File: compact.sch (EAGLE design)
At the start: 39 parts, among them J3 AVX_6-PIN_009159006061916, J4 CORTEX_DEBUG_PTH, J5 2172034-1, U1 STM32F103C8T6, U2 CJT1117-3.3-SOT223

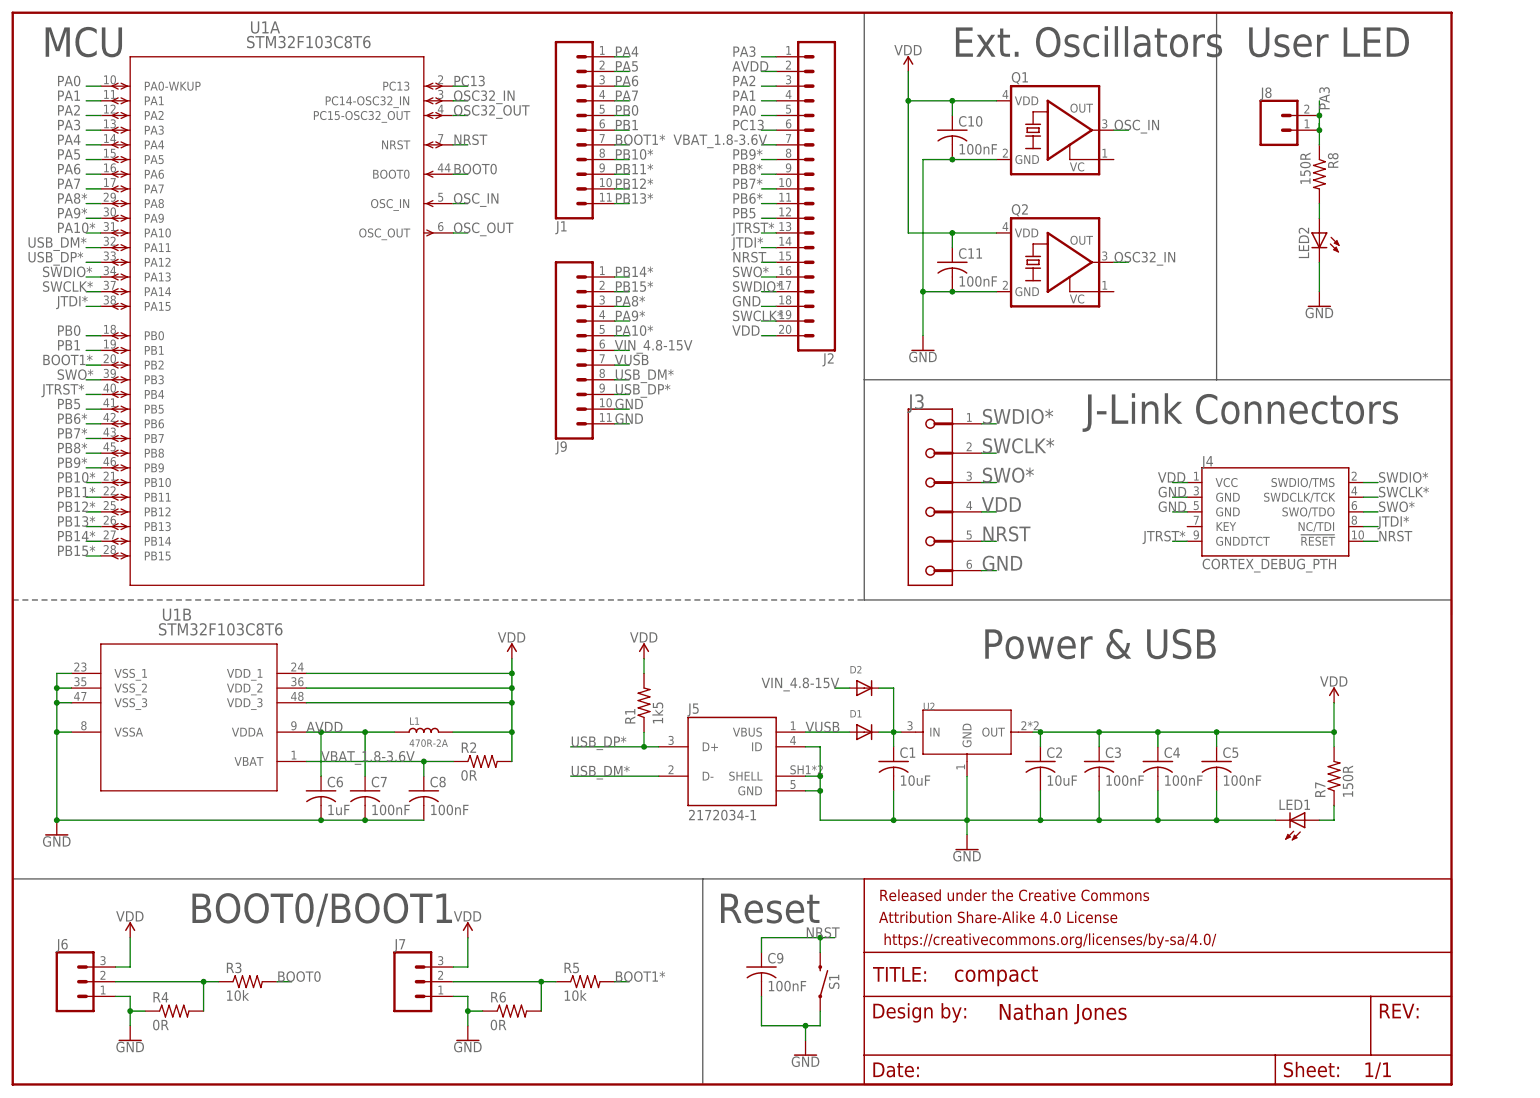
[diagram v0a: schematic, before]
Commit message: Separated Standard configuration into Standard-no-HSE and Standard-with-HSE configurations.
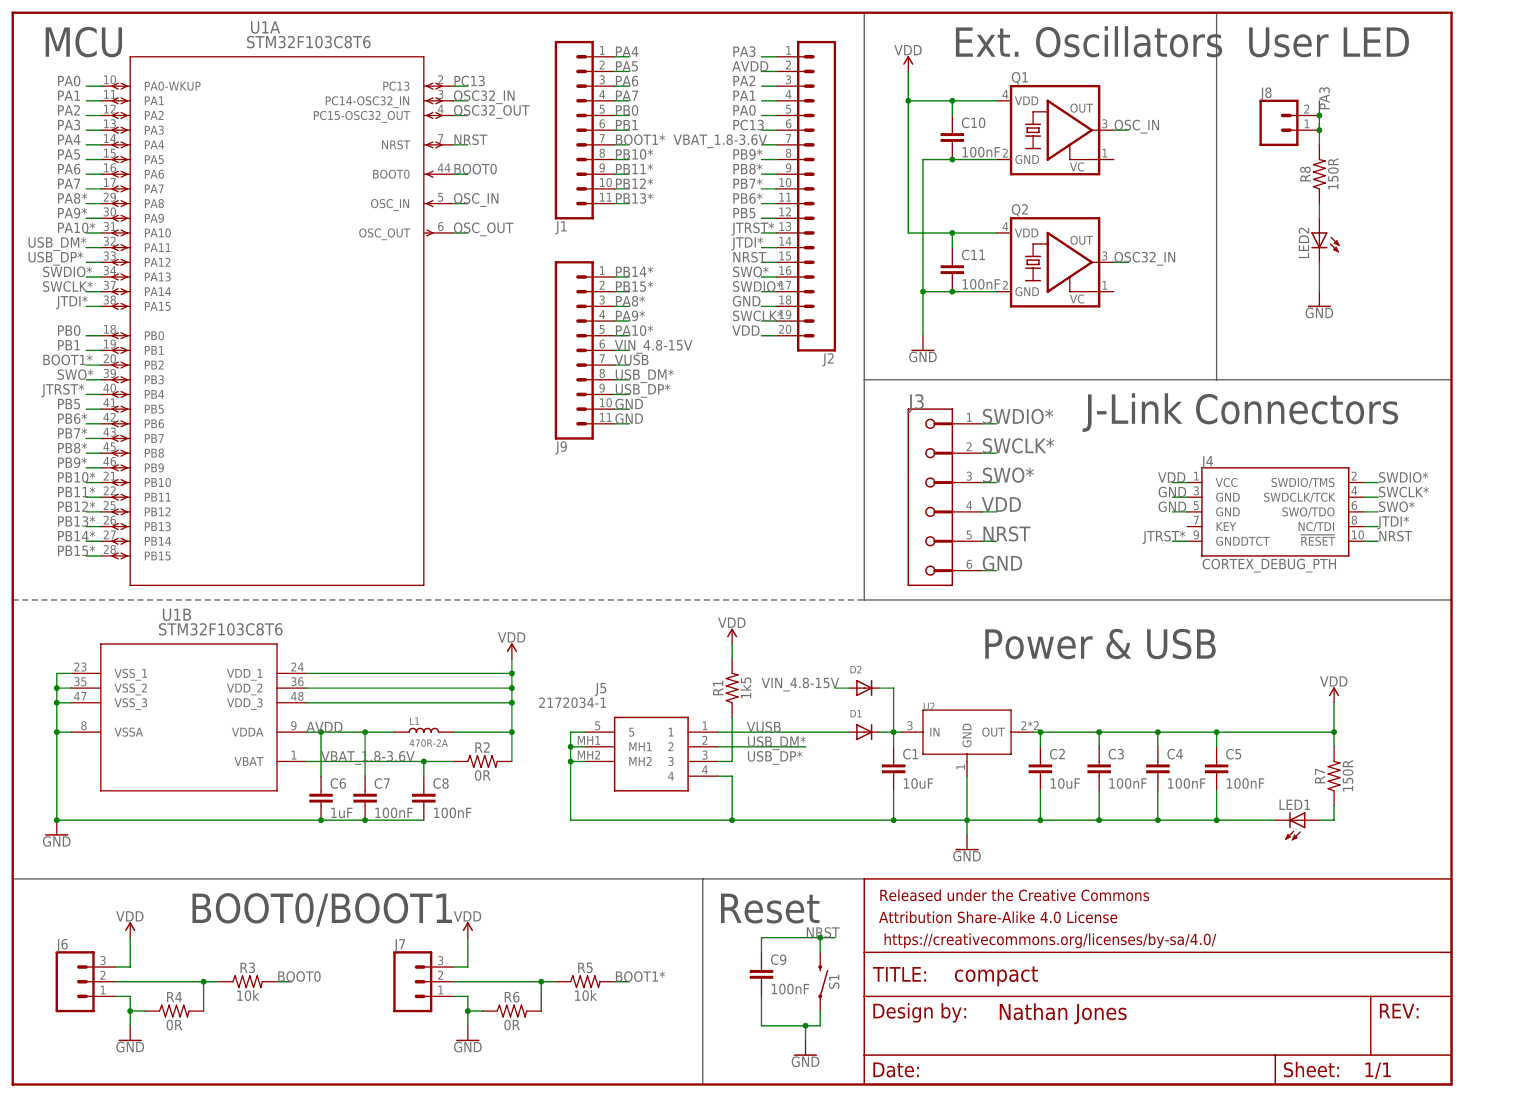
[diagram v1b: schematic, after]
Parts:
- C1, C10, C11, C2, C3, C4, C5, C6, C7, C8, C9: device adafruit:C-USC0402 -> SparkFun-Capacitors:0.1UF-0402T-16V-10%
- J5: device USB-mini-B_TE_2172034-1:2172034-1 -> 2172034-1:2172034-1
- R1, R2, R3, R4, R5, R6, R7, R8: device adafruit:R-US_R0402 -> SparkFun-Resistors:RESISTOR0402
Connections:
- net GND: now also J5.4, J5.5, J5.MH1, J5.MH2; no longer J5.GND, J5.ID, J5.SHELL
- net N$4: now also R8.1; no longer R8.2
- net PA3: now also R8.2; no longer R8.1
- net USB_DM*: now also J5.2; no longer J5.D-
- net USB_DP*: now also J5.3; no longer J5.D+
- net VUSB: now also J5.1; no longer J5.VBUS
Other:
- moved on the sheet: R1, R8

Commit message: Updated Debug Edge library. Updated Gerbers, screenshots, and schematic image. Switched to new Mini-B USB footprint.
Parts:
- J3: value AVX_6-PIN_009159006061916 -> AVX_6-PIN_009159006061916_33MIL-GAP; device Debug-Edge_AVX-connectors:AVX_6-PIN_009159006061916 -> Debug-Edge_AVX-connectors:AVX_6-PIN_009159006061916_33MIL-GAP
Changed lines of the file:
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@@
 <grid distance="0.1" unitdist="inch" unit="inch" style="lines" multiple="1" display="no" altdistance="0.01" altunitdist="inch" altunit="inch"/>
 <layers>
-<layer number="1" name="Top" color="4" fill="1" visible="no" active="no"/>
-<layer number="2" name="Route2" color="16" fill="1" visible="no" active="no"/>
-<layer number="3" name="Route3" color="17" fill="1" visible="no" active="no"/>
-<layer number="4" name="Route4" color="18" fill="1" visible="no" active="no"/>
-<layer number="5" name="Route5" color="19" fill="1" visible="no" active="no"/>
-<layer number="6" name="Route6" color="25" fill="1" visible="no" active="no"/>
-<layer number="7" name="Route7" color="26" fill="1" visible="no" active="no"/>
-<layer number="8" name="Route8" color="27" fill="1" visible="no" active="no"/>
-<layer number="9" name="Route9" color="28" fill="1" visible="no" active="no"/>
-<layer number="10" name="Route10" color="29" fill="1" visible="no" active="no"/>
-<layer number="11" name="Route11" color="30" fill="1" visible="no" active="no"/>
-<layer number="12" name="Route12" color="20" fill="1" visible="no" active="no"/>
-<layer number="13" name="Route13" color="21" fill="1" visible="no" active="no"/>
-<layer number="14" name="Route14" color="22" fill="1" visible="no" active="no"/>
-<layer number="15" name="Route15" color="23" fill="1" visible="no" active="no"/>
-<layer number="16" name="Bottom" color="1" fill="1" visible="no" active="no"/>
-<layer number="17" name="Pads" color="2" fill="1" visible="no" active="no"/>
-<layer number="18" name="Vias" color="2" fill="1" visible="no" active="no"/>
-<layer number="19" name="Unrouted" color="6" fill="1" visible="no" active="no"/>
-<layer number="20" name="Dimension" color="24" fill="1" visible="no" active="no"/>
-<layer number="21" name="tPlace" color="7" fill="1" visible="no" active="no"/>
-<layer number="22" name="bPlace" color="7" fill="1" visible="no" active="no"/>
-<layer number="23" name="tOrigins" color="15" fill="1" visible="no" active="no"/>
-<layer number="24" name="bOrigins" color="15" fill="1" visible="no" active="no"/>
-<layer number="25" name="tNames" color="7" fill="1" visible="no" active="no"/>
-<layer number="26" name="bNames" color="7" fill="1" visible="no" active="no"/>
-<layer number="27" name="tValues" color="7" fill="1" visible="no" active="no"/>
-<layer number="28" name="bValues" color="7" fill="1" visible="no" active="no"/>
+<layer number="1" name="Top" color="4" fill="1" visible="yes" active="no"/>
+<layer number="2" name="Route2" color="16" fill="1" visible="yes" active="no"/>
+<layer number="3" name="Route3" color="17" fill="1" visible="yes" active="no"/>
+<layer number="4" name="Route4" color="18" fill="1" visible="yes" active="no"/>
+<layer number="5" name="Route5" color="19" fill="1" visible="yes" active="no"/>
+<layer number="6" name="Route6" color="25" fill="1" visible="yes" active="no"/>
+<layer number="7" name="Route7" color="26" fill="1" visible="yes" active="no"/>
+<layer number="8" name="Route8" color="27" fill="1" visible="yes" active="no"/>
+<layer number="9" name="Route9" color="28" fill="1" visible="yes" active="no"/>
+<layer number="10" name="Route10" color="29" fill="1" visible="yes" active="no"/>
+<layer number="11" name="Route11" color="30" fill="1" visible="yes" active="no"/>
+<layer number="12" name="Route12" color="20" fill="1" visible="yes" active="no"/>
+<layer number="13" name="Route13" color="21" fill="1" visible="yes" active="no"/>
+<layer number="14" name="Route14" color="22" fill="1" visible="yes" active="no"/>
+<layer number="15" name="Route15" color="23" fill="1" visible="yes" active="no"/>
+<layer number="16" name="Bottom" color="1" fill="1" visible="yes" active="no"/>
+<layer number="17" name="Pads" color="2" fill="1" visible="yes" active="no"/>
+<layer number="18" name="Vias" color="2" fill="1" visible="yes" active="no"/>
+<layer number="19" name="Unrouted" color="6" fill="1" visible="yes" active="no"/>
+<layer number="20" name="Dimension" color="24" fill="1" visible="yes" active="no"/>
+<layer number="21" name="tPlace" color="7" fill="1" visible="yes" active="no"/>
+<layer number="22" name="bPlace" color="7" fill="1" visible="yes" active="no"/>
+<layer number="23" name="tOrigins" color="15" fill="1" visible="yes" active="no"/>
+<layer number="24" name="bOrigins" color="15" fill="1" visible="yes" active="no"/>
+<layer number="25" name="tNames" color="7" fill="1" visible="yes" active="no"/>
+<layer number="26" name="bNames" color="7" fill="1" visible="yes" active="no"/>
+<layer number="27" name="tValues" color="7" fill="1" visible="yes" active="no"/>
+<layer number="28" name="bValues" color="7" fill="1" visible="yes" active="no"/>
 <layer number="29" name="tStop" color="7" fill="3" visible="no" active="no"/>
 <layer number="30" name="bStop" color="7" fill="6" visible="no" active="no"/>
@@
 <layer number="35" name="tGlue" color="7" fill="4" visible="no" active="no"/>
 <layer number="36" name="bGlue" color="7" fill="5" visible="no" active="no"/>
-<layer number="37" name="tTest" color="7" fill="1" visible="no" active="no"/>
-<layer number="38" name="bTest" color="7" fill="1" visible="no" active="no"/>
+<layer number="37" name="tTest" color="7" fill="1" visible="yes" active="no"/>
+<layer number="38" name="bTest" color="7" fill="1" visible="yes" active="no"/>
 <layer number="39" name="tKeepout" color="4" fill="11" visible="no" active="no"/>
 <layer number="40" name="bKeepout" color="1" fill="11" visible="no" active="no"/>
@@
 <layer number="44" name="Drills" color="7" fill="1" visible="no" active="no"/>
 <layer number="45" name="Holes" color="7" fill="1" visible="no" active="no"/>
-<layer number="46" name="Milling" color="3" fill="1" visible="no" active="no"/>
-<layer number="47" name="Measures" color="7" fill="1" visible="no" active="no"/>
-<layer number="48" name="Document" color="7" fill="1" visible="no" active="no"/>
-<layer number="49" name="Reference" color="7" fill="1" visible="no" active="no"/>
-<layer number="50" name="dxf" color="7" fill="1" visible="no" active="no"/>
-<layer number="51" name="tDocu" color="7" fill="1" visible="no" active="no"/>
-<layer number="52" name="bDocu" color="7" fill="1" visible="no" active="no"/>
-<layer number="53" name="tGND_GNDA" color="7" fill="9" visible="no" active="no"/>
-<layer number="54" name="bGND_GNDA" color="1" fill="9" visible="no" active="no"/>
-<layer number="56" name="wert" color="7" fill="1" visible="no" active="no"/>
-<layer number="57" name="tCAD" color="7" fill="1" visible="no" active="no"/>
-<layer number="59" name="tCarbon" color="7" fill="1" visible="no" active="no"/>
-<layer number="60" name="bCarbon" color="7" fill="1" visible="no" active="no"/>
+<layer number="46" name="Milling" color="3" fill="1" visible="yes" active="no"/>
+<layer number="47" name="Measures" color="7" fill="1" visible="yes" active="no"/>
+<layer number="48" name="Document" color="7" fill="1" visible="yes" active="no"/>
+<layer number="49" name="Reference" color="7" fill="1" visible="yes" active="no"/>
+<layer number="50" name="dxf" color="7" fill="1" visible="yes" active="no"/>
+<layer number="51" name="tDocu" color="7" fill="1" visible="yes" active="no"/>
+<layer number="52" name="bDocu" color="7" fill="1" visible="yes" active="no"/>
+<layer number="53" name="tGND_GNDA" color="7" fill="9" visible="yes" active="no"/>
+<layer number="54" name="bGND_GNDA" color="1" fill="9" visible="yes" active="no"/>
+<layer number="56" name="wert" color="7" fill="1" visible="yes" active="no"/>
+<layer number="57" name="tCAD" color="7" fill="1" visible="yes" active="no"/>
+<layer number="59" name="tCarbon" color="7" fill="1" visible="yes" active="no"/>
+<layer number="60" name="bCarbon" color="7" fill="1" visible="yes" active="no"/>
 <layer number="88" name="SimResults" color="9" fill="1" visible="yes" active="yes"/>
 <layer number="89" name="SimProbes" color="9" fill="1" visible="yes" active="yes"/>
@@
 <part name="J7" library="SparkFun-Connectors" deviceset="CONN_03" device="1X03_NO_SILK"/>
 <part name="J8" library="SparkFun-Connectors" deviceset="CONN_02" device="1X02_NO_SILK"/>
-<part name="J3" library="Debug-Edge_AVX-connectors" deviceset="AVX_6-PIN_009159006061916" device=""/>
 <part name="L1" library="OPL_Ferrite_and_Magnetic_Bead" deviceset="SMD-FERRITE-BEAD-470R-2A(0805)" device="'0805'" package3d_urn="urn:adsk.eagle:package:8004624/1" value="470R-2A">
 <attribute name="LCSC_PART" value="C1015"/>
@@
 </part>
 <part name="J5" library="2172034-1" deviceset="2172034-1" device=""/>
+<part name="J3" library="Debug-Edge_AVX-connectors" deviceset="AVX_6-PIN_009159006061916_33MIL-GAP" device=""/>
 </parts>
 <sheets>
@@
 <attribute name="NAME" x="218.44" y="152.908" size="1.778" layer="95" font="vector"/>
 </instance>
-<instance part="J3" gate="G$1" x="154.94" y="106.68" smashed="yes">
-<attribute name="NAME" x="157.48" y="101.6" size="2.54" layer="95" align="top-left"/>
-</instance>
 <instance part="L1" gate="L" x="73.66" y="43.18" smashed="yes">
 <attribute name="NAME" x="71.12" y="44.45" size="1.27" layer="95" ratio="10"/>
@@
 <attribute name="VALUE" x="105.41" y="48.26" size="1.778" layer="96" rot="MR0" align="center-left"/>
 </instance>
+<instance part="J3" gate="G$1" x="154.94" y="106.68" smashed="yes">
+<attribute name="NAME" x="157.48" y="101.6" size="2.54" layer="95" align="top-left"/>
+</instance>
 </instances>
